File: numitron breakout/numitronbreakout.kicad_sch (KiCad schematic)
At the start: 13 parts, among them J1 Conn_01x06, U1 HV5812WG-G, U2 LM317_TO-220, U3 LM317_TO-220, U4 IV-12, U5 IV-12

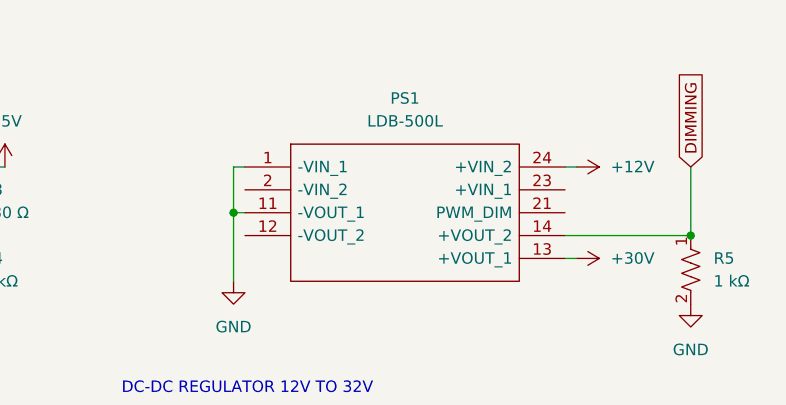
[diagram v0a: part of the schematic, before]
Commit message: updated power supply
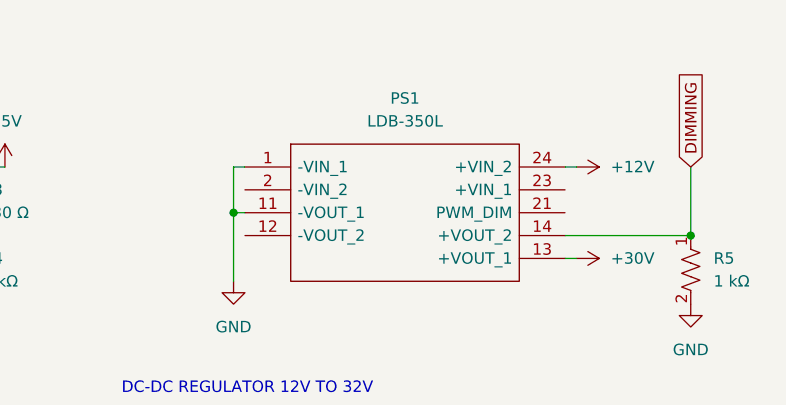
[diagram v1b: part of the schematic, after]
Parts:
- PS1: value LDB-500L -> LDB-350L; Description_1 500mA 2 ~ 32V Constant Current LED Driver Buck-Boost Topolo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 -> 350mA 2 ~ 40V Constant Current LED Driver Buck-Boost Topolo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
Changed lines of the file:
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@@
 			)
 		)
-		(property "Value" "LDB-500L"
+		(property "Value" "LDB-350L"
 			(at 209.55 33.02 0)
 			(effects
@@
 			)
 		)
-		(property "Description" "LED DVR CC BUCK-BST 2-32V 500MA"
+		(property "Description" "LED DVR CC BUCK-BST 2-40V 350MA"
 			(at 191.77 38.1 0)
 			(effects
@@
 			)
 		)
-		(property "Description_1" "500mA 2 ~ 32V Constant Current LED Driver Buck-Boost Topology 1 Output"
+		(property "Description_1" "350mA 2 ~ 40V Constant Current LED Driver Buck-Boost Topology 1 Output"
 			(at 223.52 40.64 0)
 			(effects

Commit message: code attempt, small layout updates
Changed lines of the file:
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@@
 (kicad_sch
-	(version 20231120)
+	(version 20250114)
 	(generator "eeschema")
-	(generator_version "8.0")
+	(generator_version "9.0")
 	(paper "USLetter")
 	(title_block
@@
 		(company "AL LEVINE")
 	)
+	(text "INPUT PINS"
+		(exclude_from_sim no)
+		(at 12.7 63.5 0)
+		(effects
+			(font
+				(size 1.27 1.27)
+			)
+			(justify left bottom)
+		)
+	)
+	(text "DC-DC REGULATOR 12V TO 1.5V"
+		(exclude_from_sim no)
+		(at 63.5 63.754 0)
+		(effects
+			(font
+				(size 1.27 1.27)
+			)
+			(justify left bottom)
+		)
+	)
+	(text "DC-DC REGULATOR 12V TO 32V"
+		(exclude_from_sim no)
+		(at 178.054 63.5 0)
+		(effects
+			(font
+				(size 1.27 1.27)
+			)
+			(justify left bottom)
+		)
+	)
+	(text "DC-DC REGULATOR 12V TO 5V"
+		(exclude_from_sim no)
+		(at 127 63.754 0)
+		(effects
+			(font
+				(size 1.27 1.27)
+			)
+			(justify left bottom)
+		)
+	)
+	(text "NUMITRON CONTROLLER"
+		(exclude_from_sim no)
+		(at 12.954 165.1 0)
+		(effects
+			(font
+				(size 1.27 1.27)
+			)
+			(justify left bottom)
+		)
+	)
+	(text_box "IV-12 ELECTRICAL DATA\n\nFILAMENT CURRENT		100±10 mA\nANODE SEGMENT CURRENT	≤0.8mA\nTOTAL ANODE CURRENT		3.5-5mA\nGRID CURRENT			12-17mA\n\nFILAMENT VOLTAGE		1.5±0.15V\nANODE SEGMENT & GRID VOLTAGE\n	STATIC MODE			25-30V\n	PULSE MODE			50-70V"
+		(exclude_from_sim no)
+		(at 12.7 177.8 0)
+		(size 50.8 25.4)
+		(margins 0.9524 0.9524 0.9524 0.9524)
+		(stroke
+			(width -0.0001)
+			(type default)
+		)
+		(fill
+			(type none)
+		)
+		(effects
+			(font
+				(size 1.27 1.27)
+			)
+			(justify left top)
+		)
+	)
 	(junction
 		(at 241.3 45.72)
@@
 		)
 	)
-	(text_box "IV-12 ELECTRICAL DATA\n\nFILAMENT CURRENT		100±10 mA\nANODE SEGMENT CURRENT	≤0.8mA\nTOTAL ANODE CURRENT		3.5-5mA\nGRID CURRENT			12-17mA\n\nFILAMENT VOLTAGE		1.5±0.15V\nANODE SEGMENT & GRID VOLTAGE\n	STATIC MODE			25-30V\n	PULSE MODE			50-70V"
-		(exclude_from_sim no)
-		(at 12.7 177.8 0)
-		(size 50.8 25.4)
-		(stroke
-			(width -0.0001)
-			(type default)
-		)
-		(fill
-			(type none)
-		)
-		(effects
-			(font
-				(size 1.27 1.27)
-			)
-			(justify left top)
-		)
-	)
-	(text "INPUT PINS"
-		(exclude_from_sim no)
-		(at 12.7 63.5 0)
-		(effects
-			(font
-				(size 1.27 1.27)
-			)
-			(justify left bottom)
-		)
-	)
-	(text "DC-DC REGULATOR 12V TO 1.5V"
-		(exclude_from_sim no)
-		(at 63.5 63.754 0)
-		(effects
-			(font
-				(size 1.27 1.27)
-			)
-			(justify left bottom)
-		)
-	)
-	(text "DC-DC REGULATOR 12V TO 32V"
-		(exclude_from_sim no)
-		(at 178.054 63.5 0)
-		(effects
-			(font
-				(size 1.27 1.27)
-			)
-			(justify left bottom)
-		)
-	)
-	(text "DC-DC REGULATOR 12V TO 5V"
-		(exclude_from_sim no)
-		(at 127 63.754 0)
-		(effects
-			(font
-				(size 1.27 1.27)
-			)
-			(justify left bottom)
-		)
-	)
-	(text "NUMITRON CONTROLLER"
-		(exclude_from_sim no)
-		(at 12.954 165.1 0)
-		(effects
-			(font
-				(size 1.27 1.27)
-			)
-			(justify left bottom)
-		)
-	)
 	(global_label "D_OUT"
 		(shape input)
@@
 		)
 	)
+	(embedded_fonts no)
 )

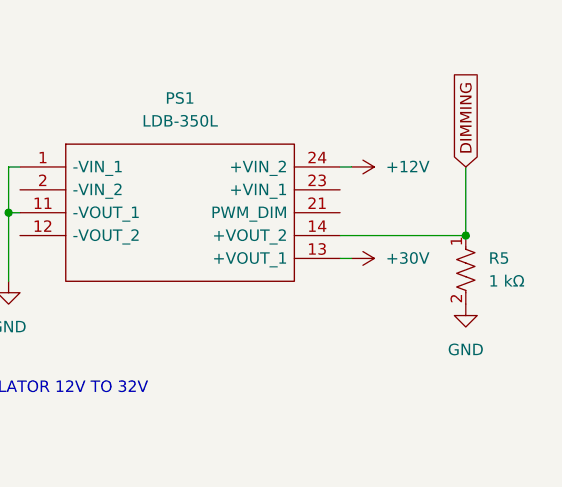
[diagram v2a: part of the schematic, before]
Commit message: fixed dimming issue
dimming pwm signal was connected to the wrong pin (VOUT2 instead of PWM_DIM) on the meanwell power supply.
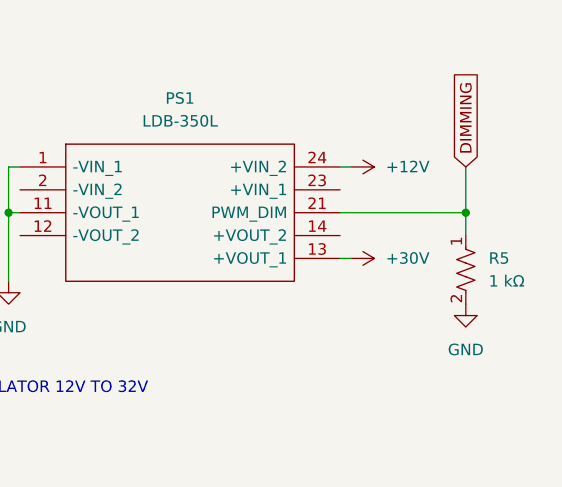
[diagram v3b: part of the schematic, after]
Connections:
- net DIMMING: now also PS1.21 (PWM_DIM); no longer PS1.14 (+VOUT_2)
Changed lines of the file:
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@@
-	)
-	(junction
-		(at 241.3 45.72)
-		(diameter 0)
-		(color 0 0 0 0)
 	)
 	(junction
@@
 	)
 	(junction
+		(at 241.3 43.18)
+		(diameter 0)
+		(color 0 0 0 0)
+	)
+	(junction
 		(at 160.02 38.1)
 		(diameter 0)
@@
 	(wire
 		(pts
-			(xy 227.33 45.72) (xy 241.3 45.72)
+			(xy 227.33 43.18) (xy 241.3 43.18)
 		)
 		(stroke
@@
 	(wire
 		(pts
-			(xy 241.3 38.1) (xy 241.3 45.72)
+			(xy 241.3 38.1) (xy 241.3 43.18)
 		)
 		(stroke
@@
 		)
 		(stroke
+			(width 0)
+			(type default)
+		)
+	)
+	(wire
+		(pts
+			(xy 241.3 43.18) (xy 241.3 45.72)
+		)
+		(stroke
